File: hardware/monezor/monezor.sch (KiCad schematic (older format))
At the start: 56 parts, among them J1 Programmer, J2 USB_C_Receptacle, J3 Display_module, SW1 SW_Push, SW2 SW_Push, U1 ATAES132A, U2 STM32F205RET6, U3 ATECC508A, U4 MCP1703A-3302_SOT23, U5 ATECC108A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

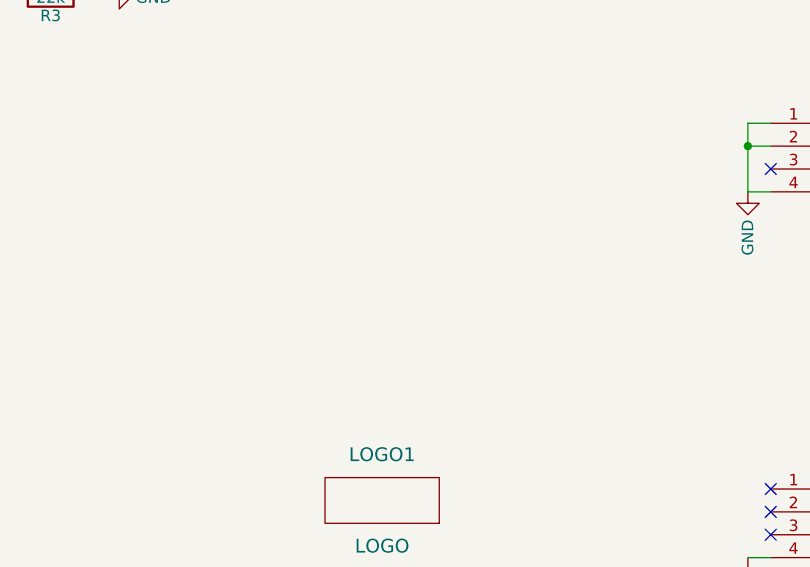
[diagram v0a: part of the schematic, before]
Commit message: Remaked panelization, added fiducials, generated new manufacturing data
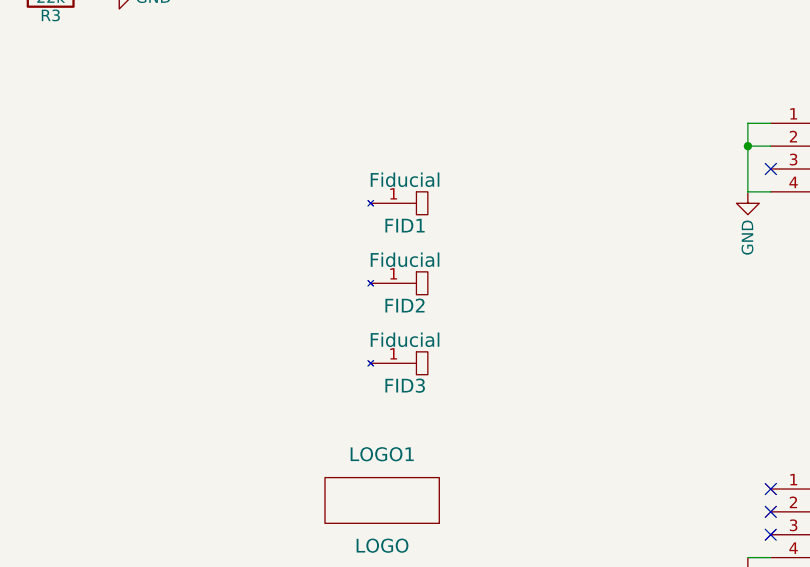
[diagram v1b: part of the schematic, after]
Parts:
- added FID1, FID2, FID3: Fiducial, monezor_footprints:Fiducial_Modern_SilkscreenTop, symbol Fiducial
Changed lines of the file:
@@
+	1    0    0    -1
+$EndComp
+$Comp
+L Fiducial FID1
+U 1 1 5A132752
+P 8700 5050
+F 0 "FID1" H 8700 4950 60  0000 C CNN
+F 1 "Fiducial" H 8700 5150 60  0000 C CNN
+F 2 "monezor_footprints:Fiducial_Modern_SilkscreenTop" H 8600 4950 60  0001 C CNN
+F 3 "" H 8600 4950 60  0001 C CNN
+	1    8700 5050
+	1    0    0    -1
+$EndComp
+$Comp
+L Fiducial FID2
+U 1 1 5A132940
+P 8700 5400
+F 0 "FID2" H 8700 5300 60  0000 C CNN
+F 1 "Fiducial" H 8700 5500 60  0000 C CNN
+F 2 "monezor_footprints:Fiducial_Modern_SilkscreenTop" H 8600 5300 60  0001 C CNN
+F 3 "" H 8600 5300 60  0001 C CNN
+	1    8700 5400
+	1    0    0    -1
+$EndComp
+$Comp
+L Fiducial FID3
+U 1 1 5A132A0A
+P 8700 5750
+F 0 "FID3" H 8700 5650 60  0000 C CNN
+F 1 "Fiducial" H 8700 5850 60  0000 C CNN
+F 2 "monezor_footprints:Fiducial_Modern_SilkscreenTop" H 8600 5650 60  0001 C CNN
+F 3 "" H 8600 5650 60  0001 C CNN
+	1    8700 5750
 	1    0    0    -1
 $EndComp
